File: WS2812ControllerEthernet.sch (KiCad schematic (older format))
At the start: 7 parts, among them J1 Conn_01x04_Male, J2 Conn_01x03_Male, J3 Conn_01x04_Male, U1 WT32_ETH01

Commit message: First release, ready to order
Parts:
- added J4: Conn_01x02_Male, Connector_PinHeader_2.54mm:PinHeader_1x02_P2.54mm_Vertical, symbol Connector:Conn_01x02_Male
- F1: footprint (none) -> halibs:Fuse-PTF75_Stelvio
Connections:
- net GND: now also J4.1 (Pin_1)
- net IO0: now reaches U1.16 (IO0)
- net IO0: now also J4.2 (Pin_2)
- net SUPPLY: now reaches F1.2, J1.1 (Pin_1), J1.2 (Pin_2)
- no-connect marks 19 -> 18
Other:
- note added: "Flashing"
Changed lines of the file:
@@
 F 0 "F1" V 2003 1250 50  0000 C CNN
 F 1 "Fuse" V 2094 1250 50  0000 C CNN
-F 2 "" V 2130 1250 50  0001 C CNN
+F 2 "halibs:Fuse-PTF75_Stelvio" V 2130 1250 50  0001 C CNN
 F 3 "~" H 2200 1250 50  0001 C CNN
 	1    2200 1250
@@
 DATA
 NoConn ~ 4000 4050
-NoConn ~ 4000 3750
 NoConn ~ 4000 3650
 NoConn ~ 4000 3550
@@
 NoConn ~ 3100 3650
 NoConn ~ 3100 3750
-NoConn ~ 3100 3450
+Text Label 1750 1250 0    50   ~ 0
+SUPPLY
+NoConn ~ 4000 3750
+Text GLabel 2850 3450 0    50   Input ~ 0
+IO0
+Wire Wire Line
+	2850 3450 3100 3450
+Text GLabel 4500 6350 0    50   Output ~ 0
+IO0
+$Comp
+L power:GND #PWR011
+U 1 1 609E1B66
+P 4900 6650
+F 0 "#PWR011" H 4900 6400 50  0001 C CNN
+F 1 "GND" H 4905 6477 50  0000 C CNN
+F 2 "" H 4900 6650 50  0001 C CNN
+F 3 "" H 4900 6650 50  0001 C CNN
+	1    4900 6650
+	1    0    0    -1
+$EndComp
+$Comp
+L Connector:Conn_01x02_Male J4
+U 1 1 609E3035
+P 5400 6450
+F 0 "J4" H 5372 6332 50  0000 R CNN
+F 1 "Conn_01x02_Male" H 5372 6423 50  0000 R CNN
+F 2 "Connector_PinHeader_2.54mm:PinHeader_1x02_P2.54mm_Vertical" H 5400 6450 50  0001 C CNN
+F 3 "~" H 5400 6450 50  0001 C CNN
+	1    5400 6450
+	-1   0    0    1
+$EndComp
+Wire Wire Line
+	5200 6450 4900 6450
+Wire Wire Line
+	4900 6450 4900 6650
+Wire Wire Line
+	5200 6350 4500 6350
+Wire Notes Line
+	4200 7000 6200 7000
+Wire Notes Line
+	6200 7000 6200 6050
+Wire Notes Line
+	6200 6050 4200 6050
+Wire Notes Line
+	4200 6050 4200 7000
+Text Notes 4200 6050 0    50   ~ 0
+Flashing
 $EndSCHEMATC

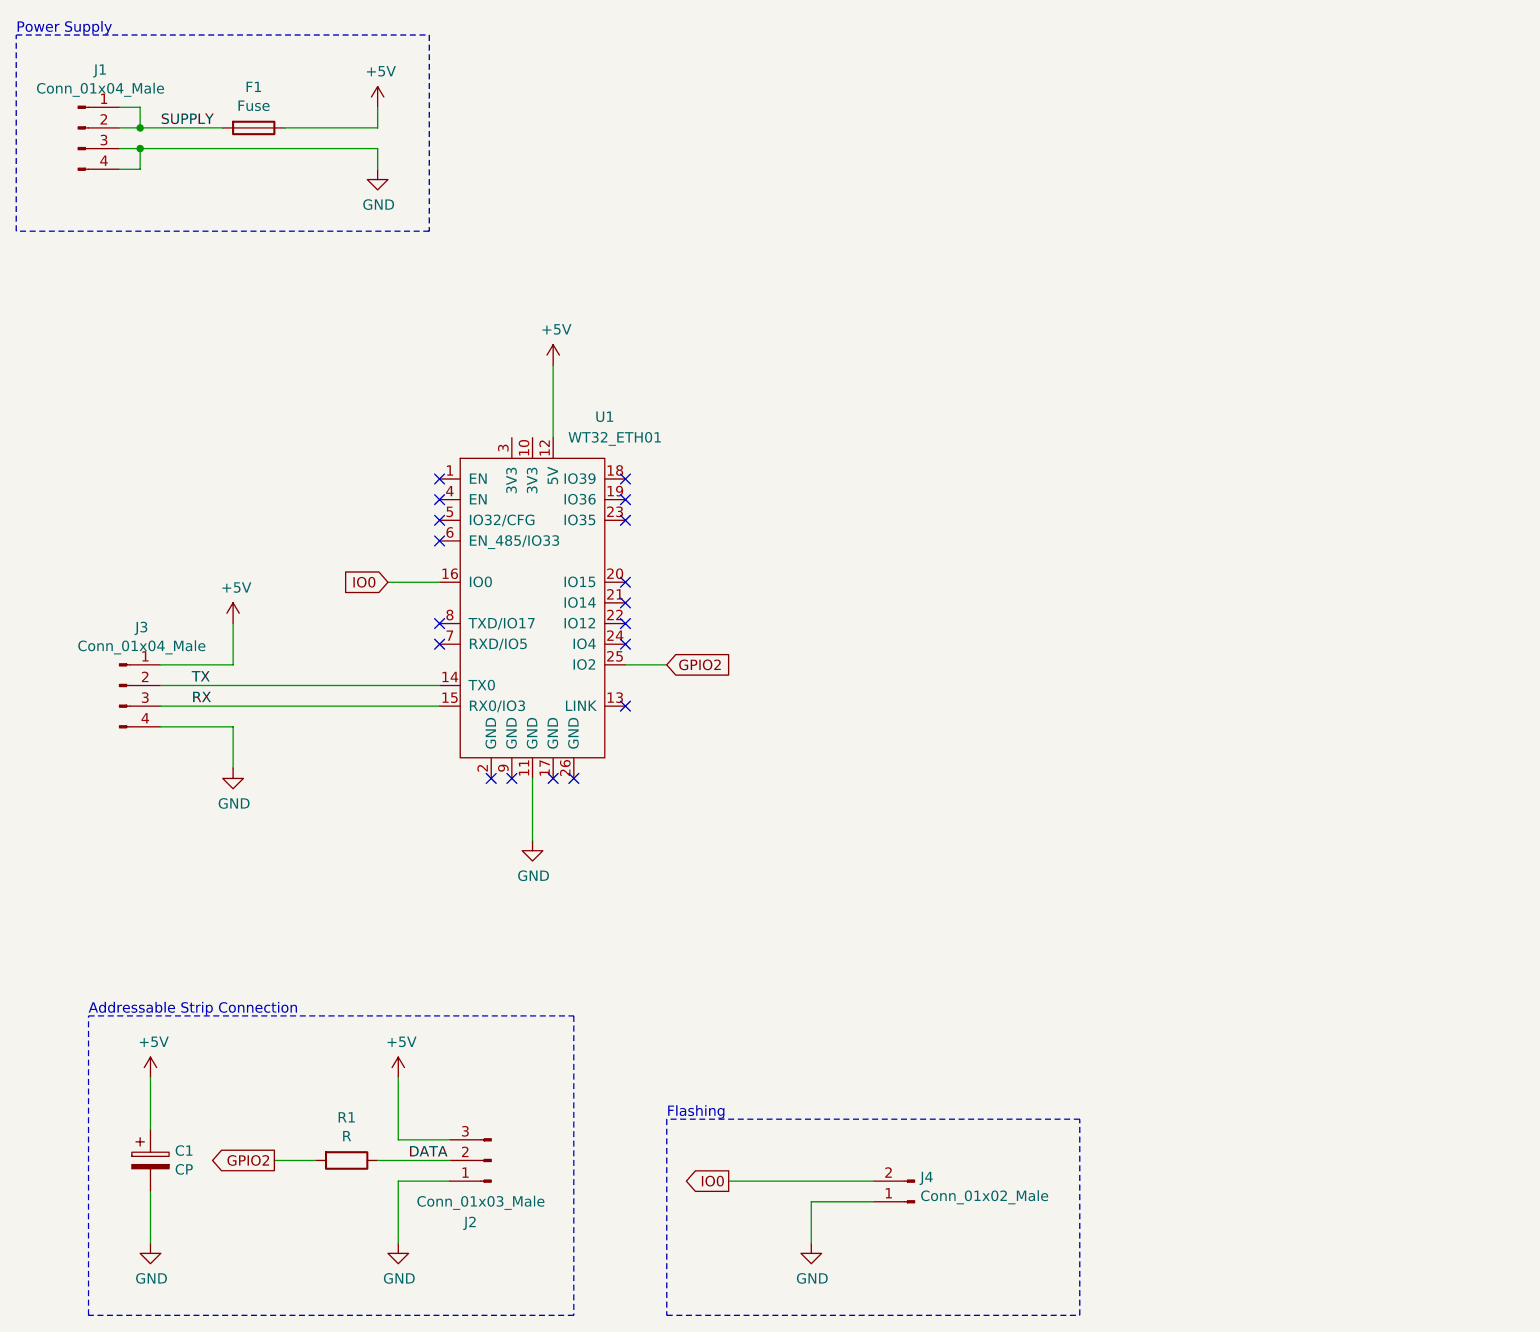
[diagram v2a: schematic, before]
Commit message: Added level shifter
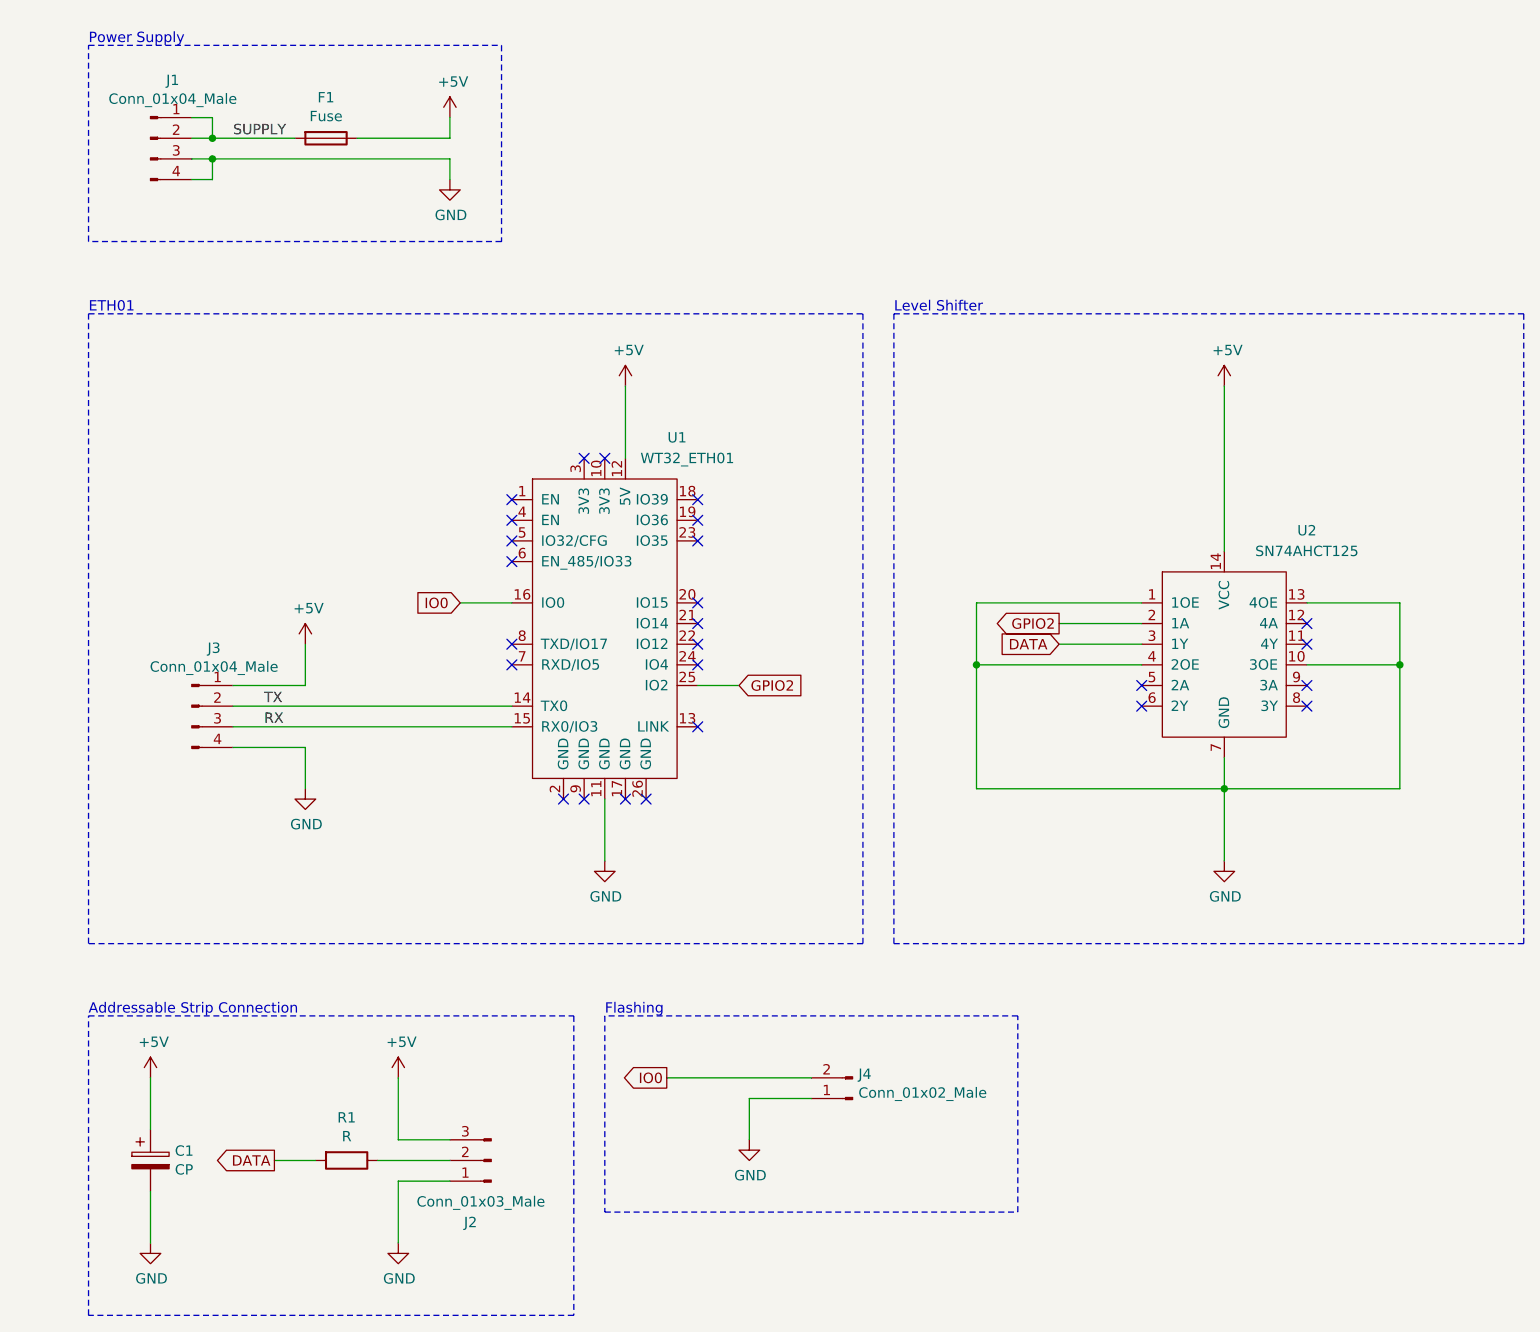
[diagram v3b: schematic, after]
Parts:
- added U2: SN74AHCT125, halibs:SN74AHCT125D, symbol haus-automatisierung:SN74AHCT125
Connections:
- net +5V: now also U2.14 (VCC)
- net DATA: now also R1.2, U2.3 (1Y); no longer J2.2 (Pin_2), R1.1
- net GND: now also U2.1 (1OE), U2.10 (3OE), U2.13 (4OE), U2.4 (2OE), U2.7 (GND)
- net GPIO2: now also U2.2 (1A); no longer R1.2
- new net: J2.2 (Pin_2), R1.1
- no-connect marks 18 -> 26
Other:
- note added: "ETH01"
- note added: "Level Shifter"
- moved on the sheet: F1, J1, J3, J4, U1
